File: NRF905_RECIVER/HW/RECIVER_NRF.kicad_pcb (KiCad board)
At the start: 2 copper layers, 21 parts, among them J1 Conn_Coaxial, U1 NRF905, U2 3.2_ILI9341_16bit, U3 ESP-07, Y1 Crystal

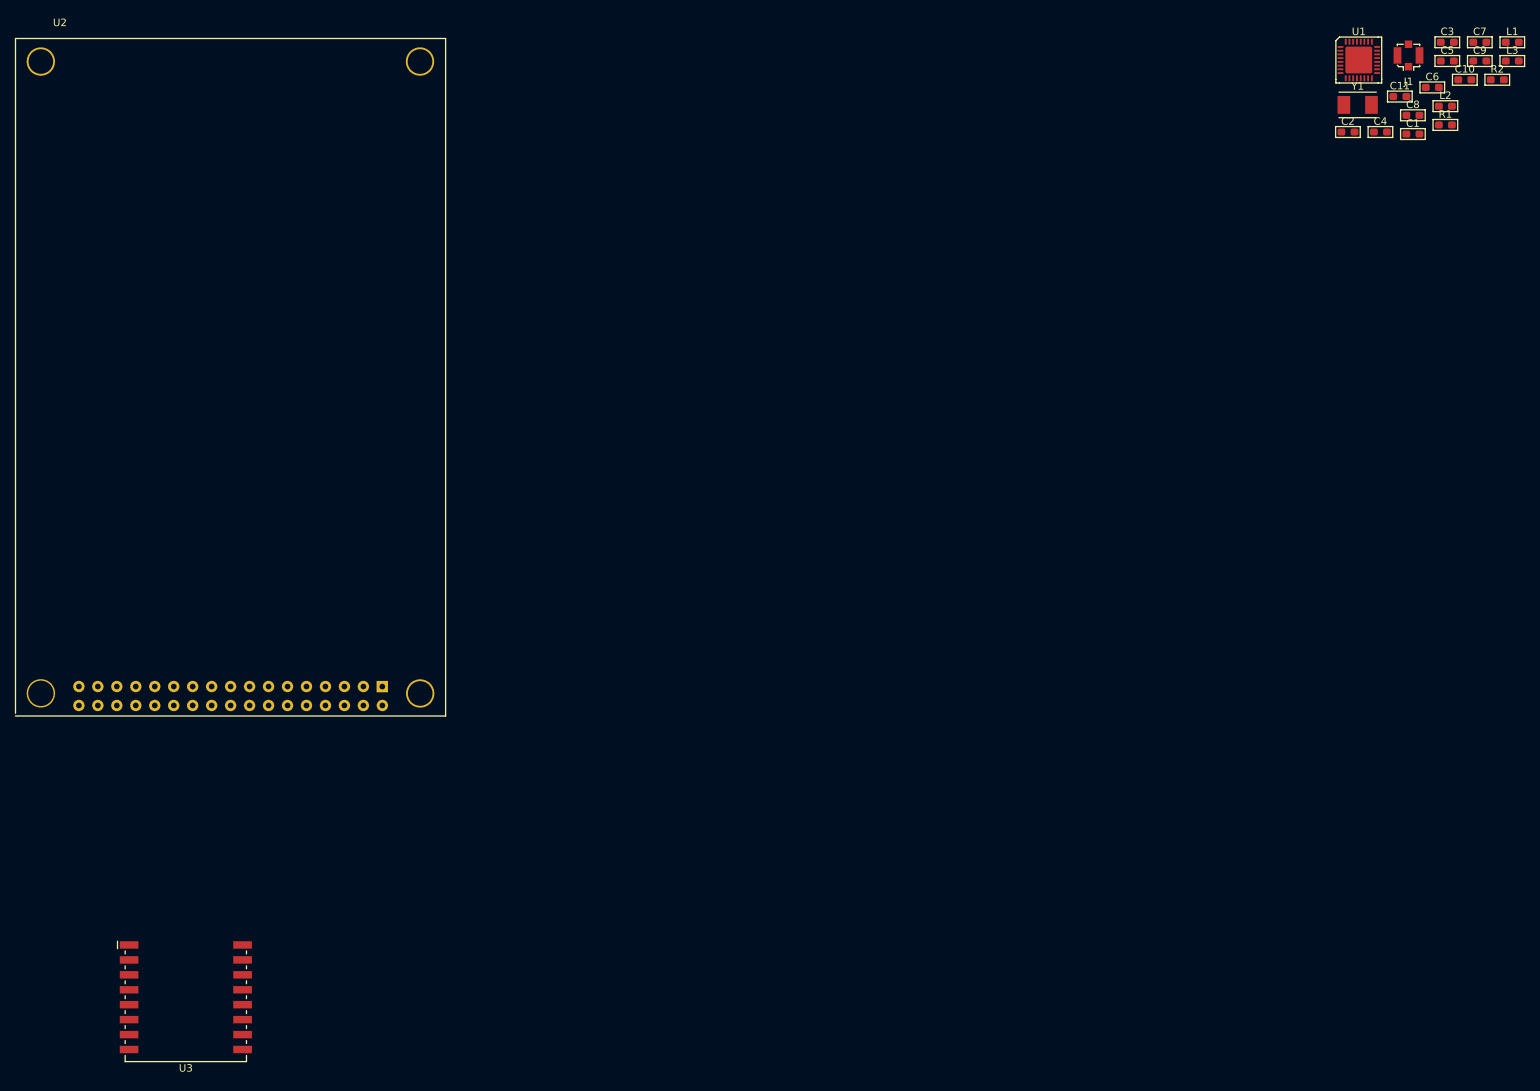
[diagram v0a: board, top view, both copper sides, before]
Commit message: Изменена структура проека. Добавлен шаблон проекта для ESP32. Изменение в схемотехнике WIFI модуль с ESP-07 изменени на ESP32 WROVER-IB
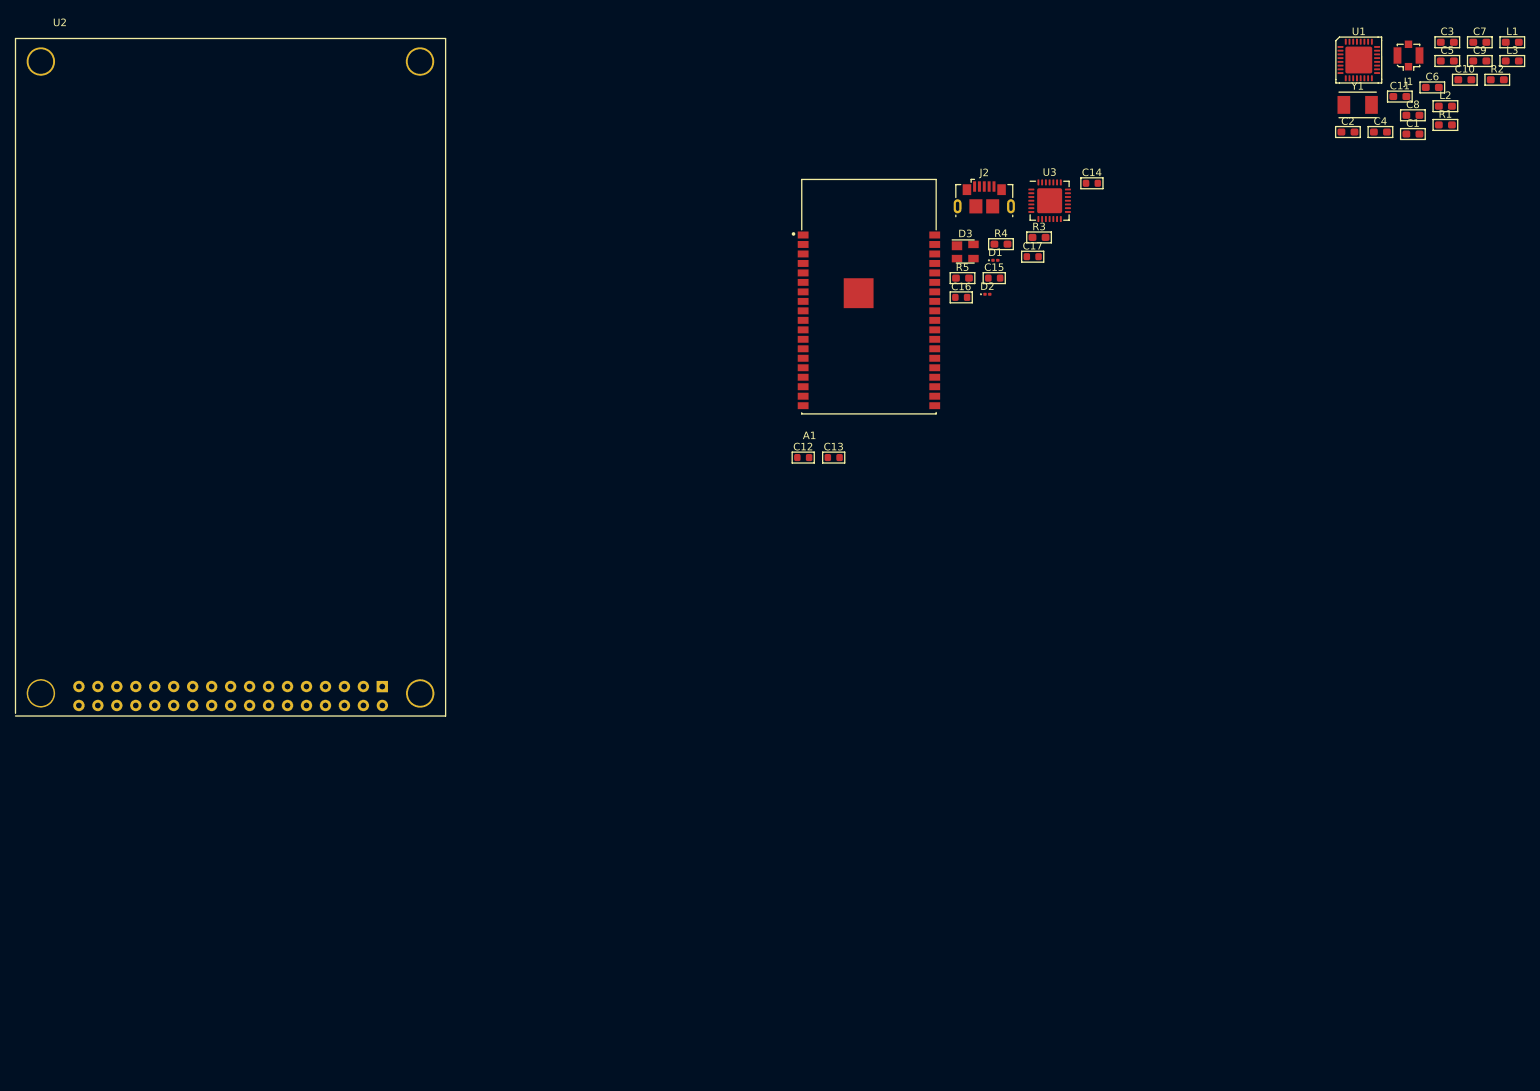
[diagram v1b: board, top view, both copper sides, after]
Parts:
- added A1: ESP32-WROVER-I, ESP32 WROVER-IB:ESP32-WROVER-IB, F.Cu at (179.9, 55.9)
- added C12: C, Capacitor_SMD:C_0603_1608Metric, F.Cu at (171.9, 77.4)
- added C13: C, Capacitor_SMD:C_0603_1608Metric, F.Cu at (176.0, 77.4)
- added C14: C, Capacitor_SMD:C_0603_1608Metric, F.Cu at (210.6, 40.6)
- added C15: C, Capacitor_SMD:C_0603_1608Metric, F.Cu at (197.5, 53.3)
- added C16: C, Capacitor_SMD:C_0603_1608Metric, F.Cu at (193.1, 55.9)
- added C17: C, Capacitor_SMD:C_0603_1608Metric, F.Cu at (202.7, 50.5)
- added D1: LED, LED_SMD:LED_0201_0603Metric, F.Cu at (197.7, 51.0)
- added D2: LED, LED_SMD:LED_0201_0603Metric, F.Cu at (196.6, 55.5)
- added D3: SP0503BAHT, Package_TO_SOT_SMD:SOT-143, F.Cu at (193.6, 49.8)
- added J2: USB_B_Micro, Connector_USB:USB_Micro-B_GCT_USB3076-30-A, F.Cu at (196.2, 42.5)
- added R3: R, Resistor_SMD:R_0603_1608Metric_Pad1.05x0.95mm_HandSolder, F.Cu at (203.5, 47.9)
- added R4: R, Resistor_SMD:R_0603_1608Metric_Pad1.05x0.95mm_HandSolder, F.Cu at (198.4, 48.8)
- added R5: R, Resistor_SMD:R_0603_1608Metric_Pad1.05x0.95mm_HandSolder, F.Cu at (193.3, 53.3)
- U3: value ESP-07 -> CP2102N-A01-GQFN28; footprint RF_Module:ESP-07 -> Package_DFN_QFN:QFN-28-1EP_5x5mm_P0.5mm_EP3.35x3.35mm
- moved U3 155.9 mm to (204.9, 43.0)
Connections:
- net /NRF905/VDD_P renamed /NRF905/VDD_NRF
- U2 pad 24: (no net) -> +3V3
- U2 pad 25: (no net) -> +3V3
- U2 pad 26: (no net) -> GNDREF
- U2 pad 27: (no net) -> GNDREF
- U2 pad 35: (no net) -> GNDREF
- U2 pad 36: (no net) -> GNDREF
- U2 pad 37: (no net) -> GNDREF
- U2 pad 38: (no net) -> GNDREF
- U3 pad 3: (no net) -> GNDREF
- U3 pad 4: (no net) -> Net-(D3-Pad3)
- U3 pad 5: (no net) -> Net-(D3-Pad4)
- U3 pad 6: (no net) -> /ESP32/VDD_ESP32
- U3 pad 7: (no net) -> /ESP32/VDD_ESP32
- U3 pad 8: (no net) -> Net-(D3-Pad2)
- U3 pad 9: (no net) -> Net-(R5-Pad2)
